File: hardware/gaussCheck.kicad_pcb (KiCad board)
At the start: 2 copper layers, 31.5 x 96.4 mm, 68 parts, among them J1 USB_C_Receptacle_USB2.0, J2 SWD, Q1 BSS138, Q2 BSS83P, Q3 BSS138, SW1 PTS810, SW2 PT847S, SW3 PT847S, SW4 PT847S, U1 TLV493D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

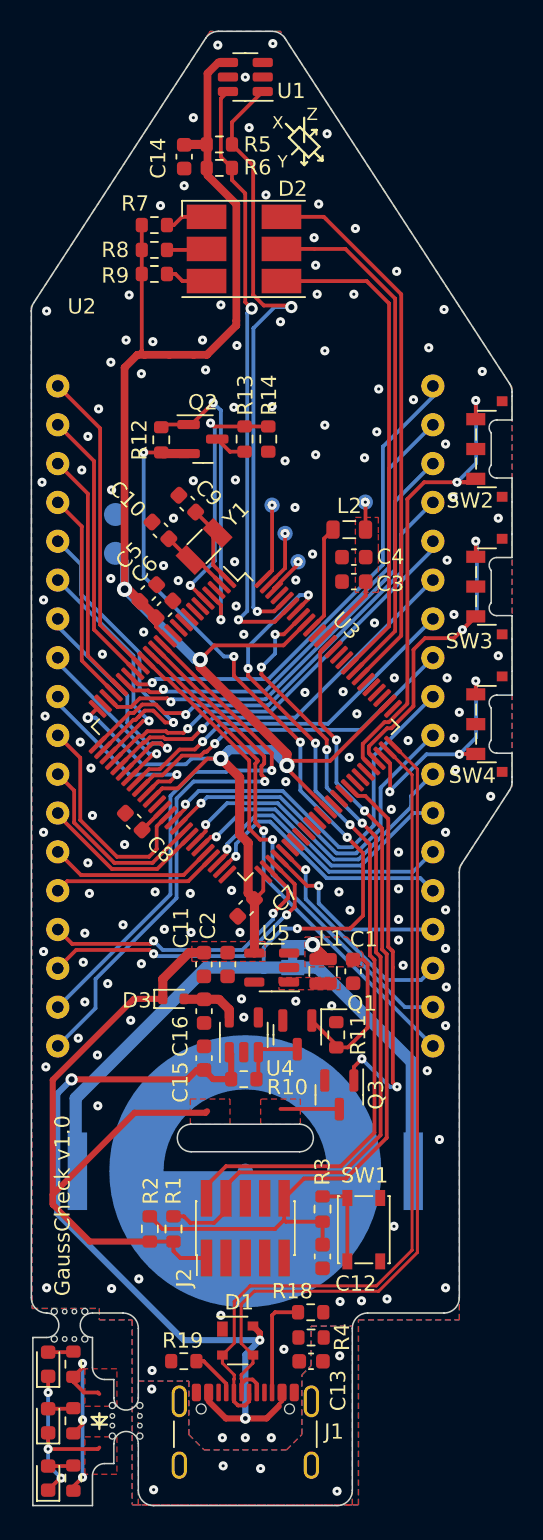
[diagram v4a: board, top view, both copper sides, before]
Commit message: updated daughter board for 1.8mm mill
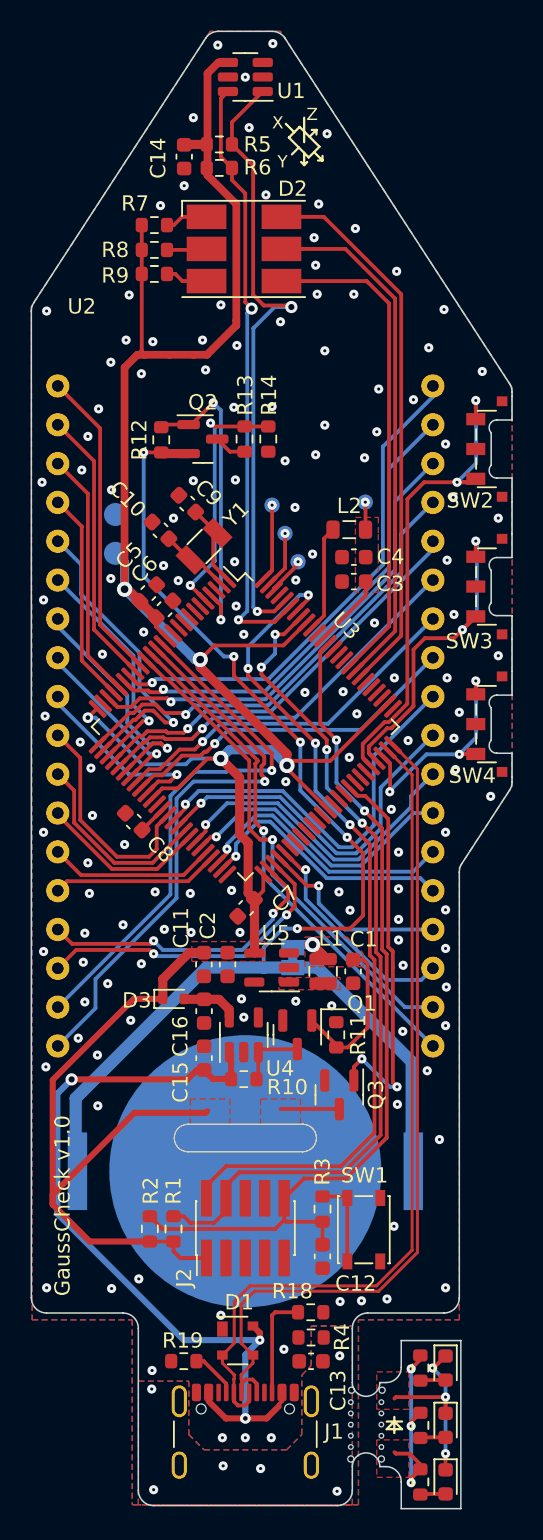
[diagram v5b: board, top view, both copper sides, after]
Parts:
- removed the REF** at (92.2, 135.8)
- removed the REF** at (88.5, 129.6)
- added REF**: MouseBite_Mill1.8mm_5.5mmwide, GaussCheckCustomFootprint:MouseBite_Mill1.8mm_5.5mmwide, F.Cu at (107.9, 136.1)
- BT1: footprint GaussCheckCustomFootprint:BatteryHolder_Keystone_3034_1x20mm_donut -> Battery:BatteryHolder_Keystone_3034_1x20mm
- moved D6 27.1 mm to (113.1, 139.8), turned to -90 degrees
- moved D4 27.0 mm to (113.1, 132.3), turned to -90 degrees
- moved D5 26.0 mm to (113.1, 136.1), turned to -90 degrees
- moved R17 24.0 mm to (111.5, 139.8), turned to -90 degrees
- moved R15 23.8 mm to (111.5, 132.3), turned to -90 degrees
- moved R16 22.7 mm to (111.5, 136.1), turned to -90 degrees
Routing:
- net GND: vias 138 -> 140
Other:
- board size 31.5 x 96.4 mm -> 31.5 x 96.7 mm
